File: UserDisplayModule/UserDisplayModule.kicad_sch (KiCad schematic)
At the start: 44 parts, among them J1 RJ45_Shielded, U1 74HC595, U2 LM324, U3 74HC595, U4 74HC595

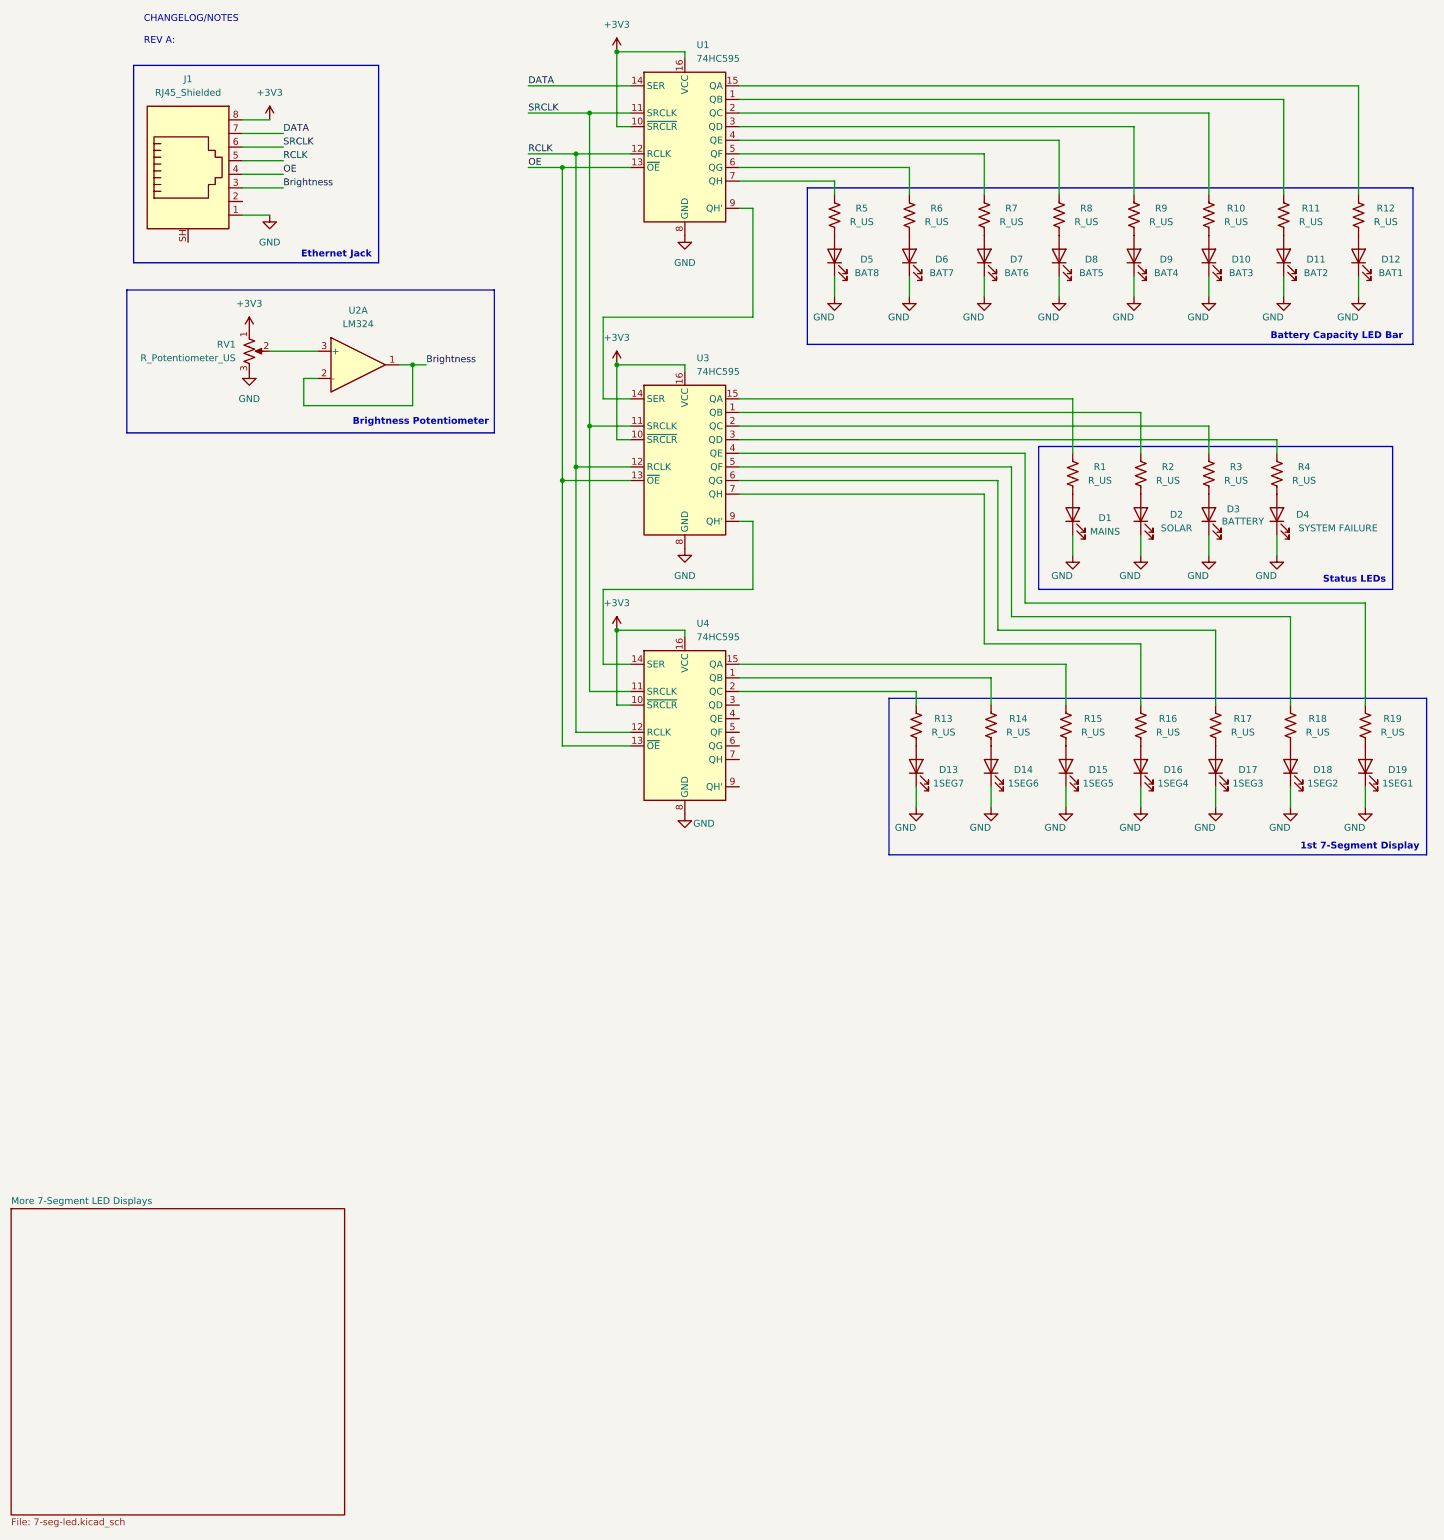
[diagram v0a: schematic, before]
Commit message: finished schematic + addressed comments
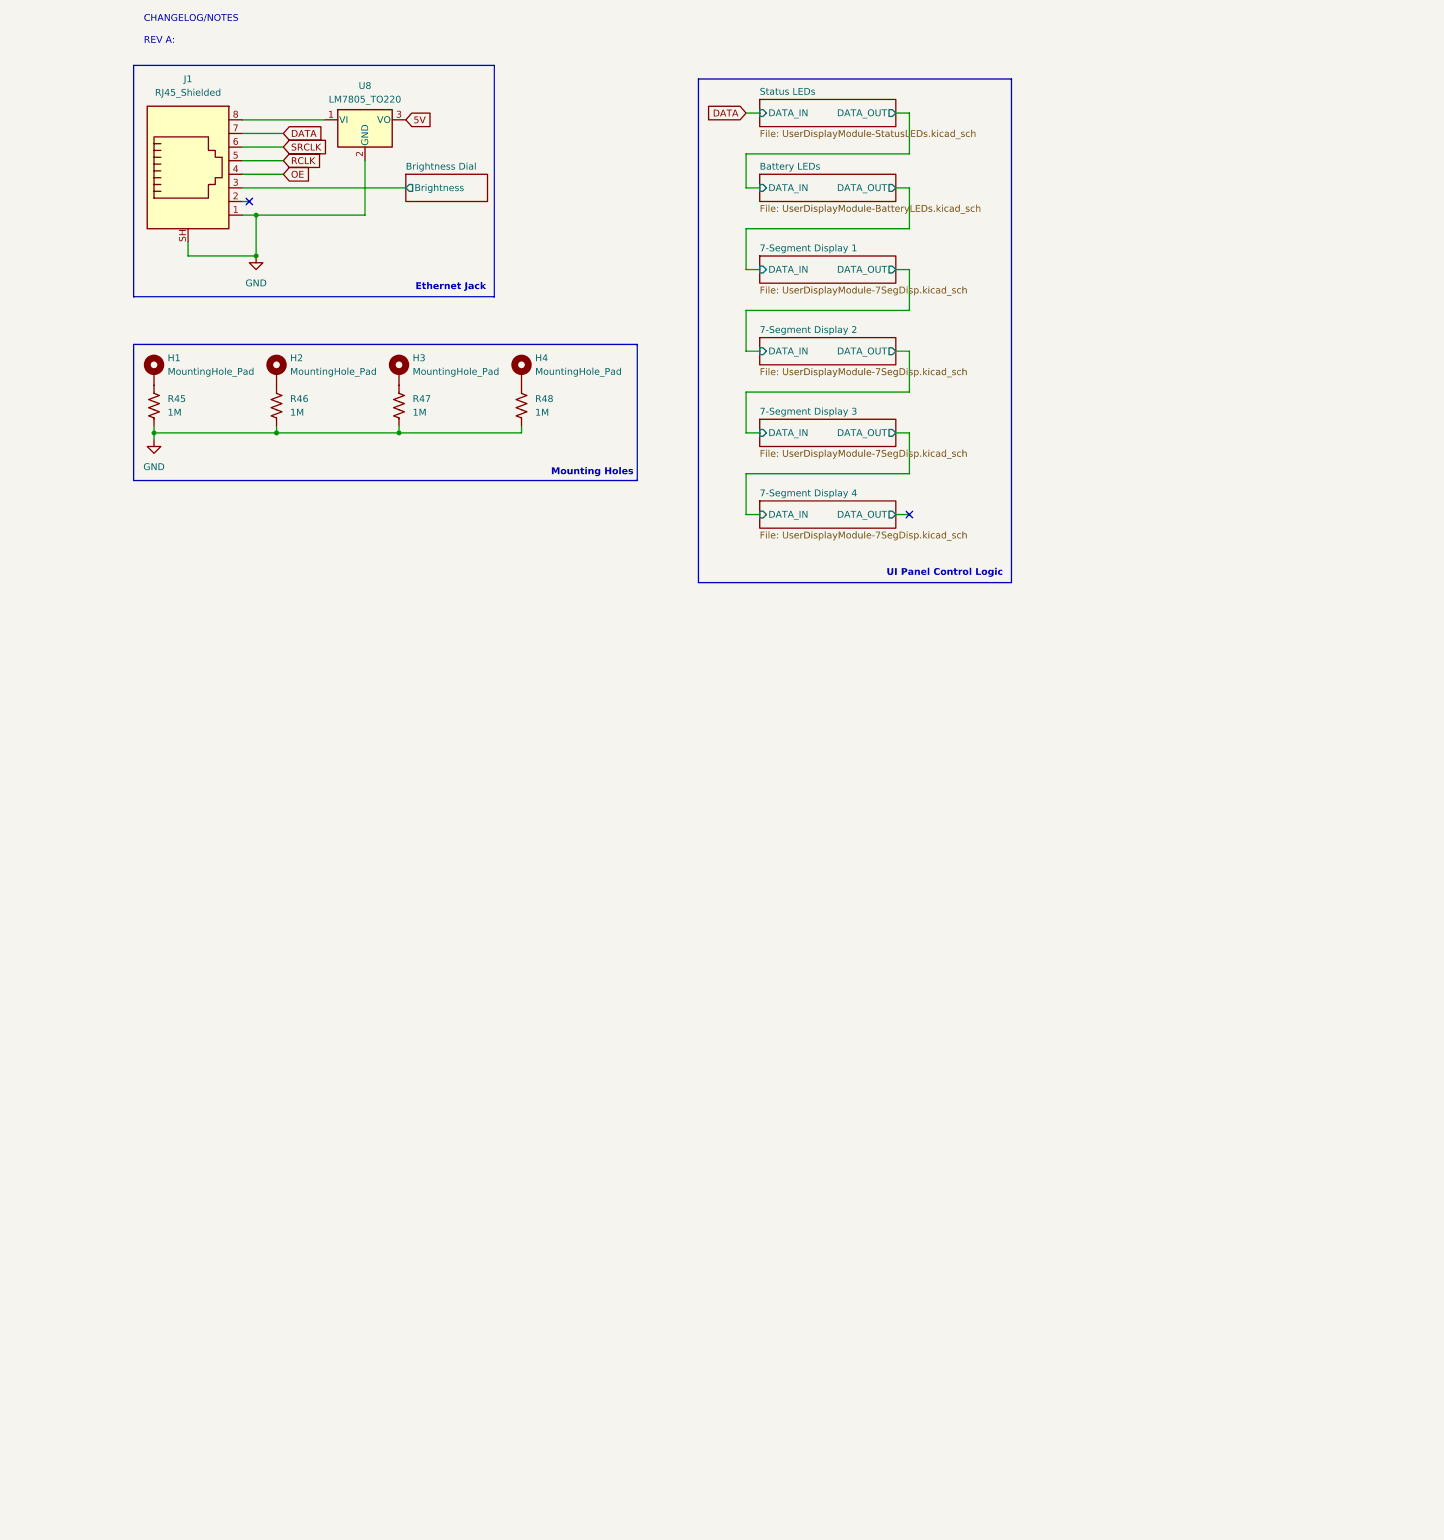
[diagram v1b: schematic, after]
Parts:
- removed D1: MAINS, symbol Device:LED
- removed D10: BAT3, symbol Device:LED
- removed D11: BAT2, symbol Device:LED
- removed D12: BAT1, symbol Device:LED
- removed D13: 1SEG7, symbol Device:LED
- removed D14: 1SEG6, symbol Device:LED
- removed D15: 1SEG5, symbol Device:LED
- removed D16: 1SEG4, symbol Device:LED
- removed D17: 1SEG3, symbol Device:LED
- removed D18: 1SEG2, symbol Device:LED
- removed D19: 1SEG1, symbol Device:LED
- removed D2: SOLAR, symbol Device:LED
- removed D3: BATTERY, symbol Device:LED
- removed D4: SYSTEM FAILURE, symbol Device:LED
- removed D5: BAT8, symbol Device:LED
- removed D6: BAT7, symbol Device:LED
- removed D7: BAT6, symbol Device:LED
- removed D8: BAT5, symbol Device:LED
- removed D9: BAT4, symbol Device:LED
- removed R1, R10, R11, R12, R13, R14, R15, R16, R17, R18, R19, R2, R3, R4, R5, R6, R7, R8, R9: R_US, symbol Device:R_US
- removed RV1: R_Potentiometer_US, symbol Device:R_Potentiometer_US
- removed U1, U3, U4: 74HC595, symbol 74xx:74HC595
- removed U2: LM324, symbol Amplifier_Operational:LM324
- added H1, H2, H3, H4: MountingHole_Pad, symbol Mechanical:MountingHole_Pad
- added R45, R46, R47, R48: 1M, symbol Device:R_US
- added U8: LM7805_TO220, Package_TO_SOT_THT:TO-220-3_Vertical, symbol Regulator_Linear:LM7805_TO220
- J1: footprint (none) -> Connector_RJ:RJ45_Shielded_EthernetJack
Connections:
- net GND: now also J1.SH, R45.2, R46.2, R47.2, R48.2, U8.2 (GND)
- net +3V3: no longer names the net of J1.8
- net +3V3: now also U8.1 (VI)
- net Brightness renamed Brightness Dial/Brightness
- new net: H4.1, R48.1
- new net: H1.1, R45.1
- new net: H2.1, R46.1
- new net: H3.1, R47.1
- new net 5V: U8.3 (VO)
- no-connect marks 0 -> 2
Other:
- removed sheet More 7-Segment LED Displays
- added sheet 7-Segment Display 1 (UserDisplayModule-7SegDisp.kicad_sch)
- added sheet 7-Segment Display 2 (UserDisplayModule-7SegDisp.kicad_sch)
- added sheet 7-Segment Display 3 (UserDisplayModule-7SegDisp.kicad_sch)
- added sheet 7-Segment Display 4 (UserDisplayModule-7SegDisp.kicad_sch)
- added sheet Battery LEDs (UserDisplayModule-BatteryLEDs.kicad_sch)
- added sheet Brightness Dial (UserDisplayModule-BrightnessDial.kicad_sch)
- added sheet Status LEDs (UserDisplayModule-StatusLEDs.kicad_sch)
- note added: "Mounting Holes"
- note added: "UI Panel Control Logic"
- note removed: "1st 7-Segment Display"
- note removed: "Battery Capacity LED Bar"
- note removed: "Brightness Potentiometer"
- note removed: "Status LEDs"

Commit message: doubled LEDs + started PCB
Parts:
- H1, H2, H3, H4: footprint (none) -> MountingHole:MountingHole_3.2mm_M3_Pad
- R45, R46, R47, R48: footprint (none) -> Resistor_SMD:R_0805_2012Metric
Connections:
- no-connect marks 2 -> 1

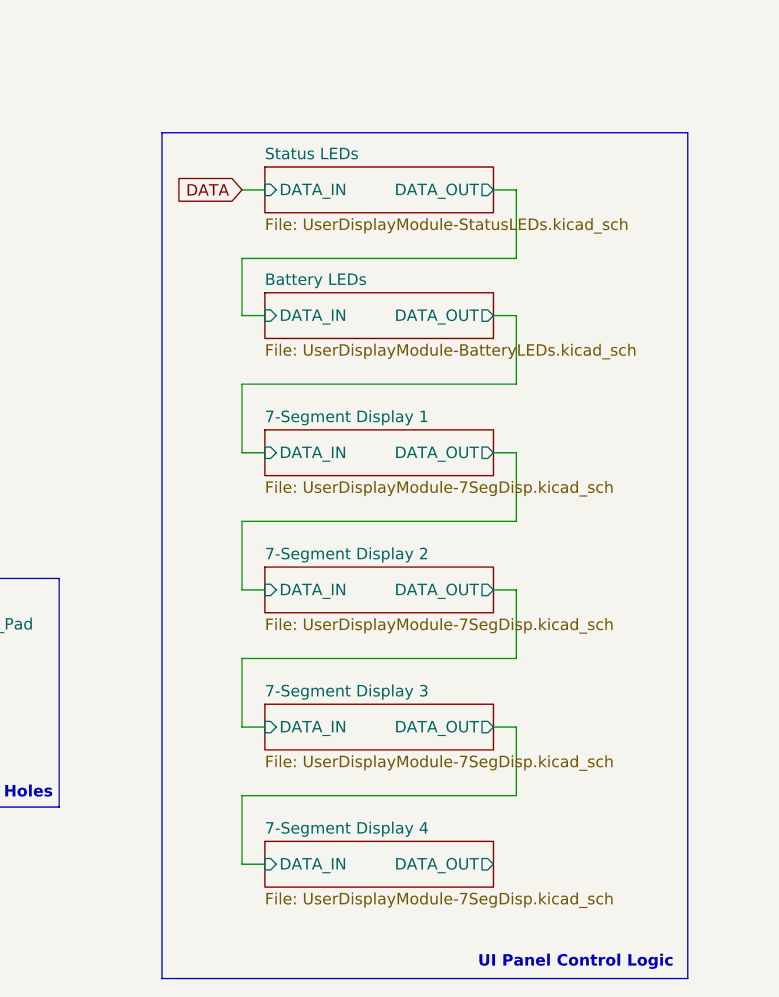
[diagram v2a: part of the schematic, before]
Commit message: finished routing pcb (minus ground pour)
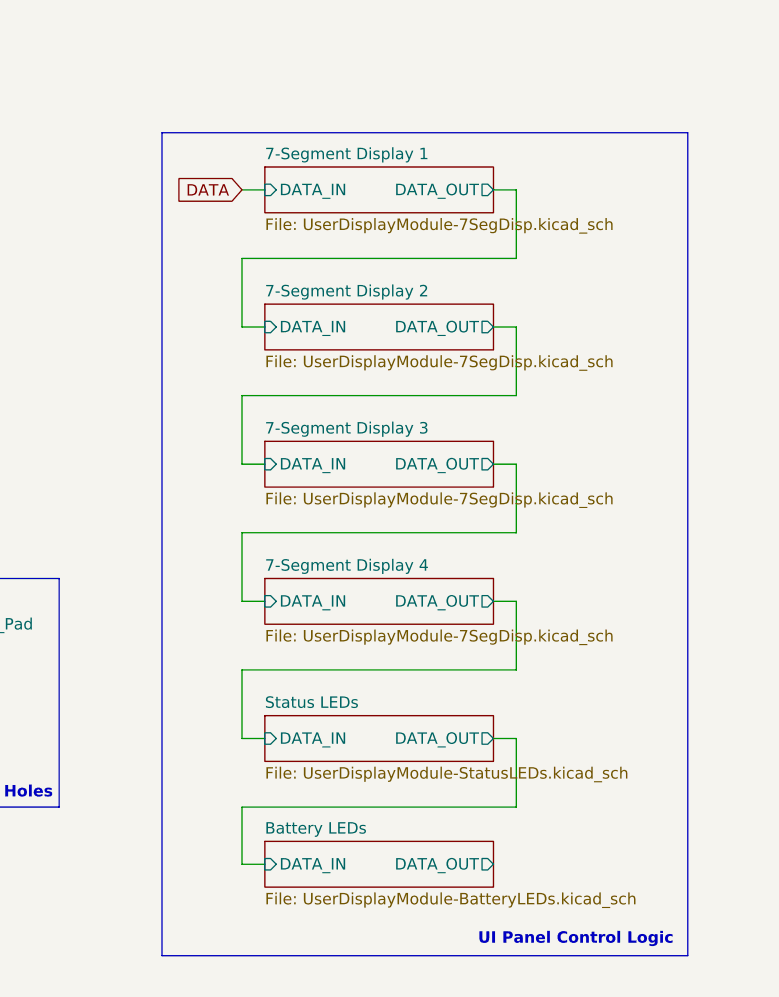
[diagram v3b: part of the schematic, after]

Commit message: added digikey pns
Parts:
- J1: Digikey PN (none) -> AE10399-ND
- U8: Digikey PN (none) -> 2129-NJM7805FA-ND
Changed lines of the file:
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@@
 	(title_block
 		(title "Main")
-		(date "2024-03-22")
+		(date "2024-04-01")
+		(rev "1")
 	)
 	(junction
@@
 			)
 		)
+		(property "Digikey PN" ""
+			(at 90.17 90.17 0)
+			(effects
+				(font
+					(size 1.27 1.27)
+				)
+				(hide yes)
+			)
+		)
 		(pin "1"
 		)
@@
 			)
 		)
+		(property "Digikey PN" ""
+			(at 21.59 90.17 0)
+			(effects
+				(font
+					(size 1.27 1.27)
+				)
+				(hide yes)
+			)
+		)
 		(pin "1"
 		)
@@
 			)
 		)
+		(property "Digikey PN" ""
+			(at 44.45 90.17 0)
+			(effects
+				(font
+					(size 1.27 1.27)
+				)
+				(hide yes)
+			)
+		)
 		(pin "1"
 		)
@@
 			)
 		)
+		(property "Digikey PN" "AE10399-ND"
+			(at 27.94 46.99 0)
+			(effects
+				(font
+					(size 1.27 1.27)
+				)
+				(hide yes)
+			)
+		)
 		(pin "6"
 		)
@@
 			)
 		)
+		(property "Digikey PN" ""
+			(at 21.59 83.82 0)
+			(effects
+				(font
+					(size 1.27 1.27)
+				)
+				(hide yes)
+			)
+		)
 		(pin "1"
 		)
@@
 			)
 		)
+		(property "Digikey PN" ""
+			(at 67.31 90.17 0)
+			(effects
+				(font
+					(size 1.27 1.27)
+				)
+				(hide yes)
+			)
+		)
 		(pin "1"
 		)
@@
 			)
 		)
+		(property "Digikey PN" ""
+			(at 90.17 83.82 0)
+			(effects
+				(font
+					(size 1.27 1.27)
+				)
+				(hide yes)
+			)
+		)
 		(pin "1"
 		)
@@
 			)
 		)
+		(property "Digikey PN" ""
+			(at 44.45 83.82 0)
+			(effects
+				(font
+					(size 1.27 1.27)
+				)
+				(hide yes)
+			)
+		)
 		(pin "1"
 		)
@@
 			)
 		)
+		(property "Digikey PN" ""
+			(at 67.31 83.82 0)
+			(effects
+				(font
+					(size 1.27 1.27)
+				)
+				(hide yes)
+			)
+		)
 		(pin "1"
 		)
@@
 			)
 		)
-		(property "Datasheet" "https://www.onsemi.cn/PowerSolutions/document/MC7800-D.PDF"
+		(property "Datasheet" "https://www.nisshinbo-microdevices.co.jp/en/pdf/datasheet/NJM7800_E.pdf"
 			(at 60.96 38.1 0)
 			(effects
@@
 			(at 60.96 36.83 0)
 			(effects
+				(font
+					(size 1.27 1.27)
+				)
+				(hide yes)
+			)
+		)
+		(property "Digikey PN" "2129-NJM7805FA-ND"
+			(at 60.96 36.83 0)
+			(effects

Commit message: Edited BOM for R/C parts
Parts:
- R45, R46, R47, R48: Digikey PN (none) -> RMCF0805FT1M00CT-ND
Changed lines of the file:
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@@
 			)
 		)
-		(property "Digikey PN" ""
+		(property "Digikey PN" "RMCF0805FT1M00CT-ND"
 			(at 90.17 90.17 0)
 			(effects
@@
 			)
 		)
-		(property "Digikey PN" ""
+		(property "Digikey PN" "RMCF0805FT1M00CT-ND"
 			(at 21.59 90.17 0)
 			(effects
@@
 			)
 		)
-		(property "Digikey PN" ""
+		(property "Digikey PN" "RMCF0805FT1M00CT-ND"
 			(at 44.45 90.17 0)
 			(effects
@@
 			)
 		)
-		(property "Digikey PN" ""
+		(property "Digikey PN" "RMCF0805FT1M00CT-ND"
 			(at 67.31 90.17 0)
 			(effects
